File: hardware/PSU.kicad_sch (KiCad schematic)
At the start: 22 parts, among them J1 UJ20-C-H-G-SMT-2A-P16-TR, U2 REF35330QDBVR, U4 LM27762, U5 NCP1117-3.3_SOT223

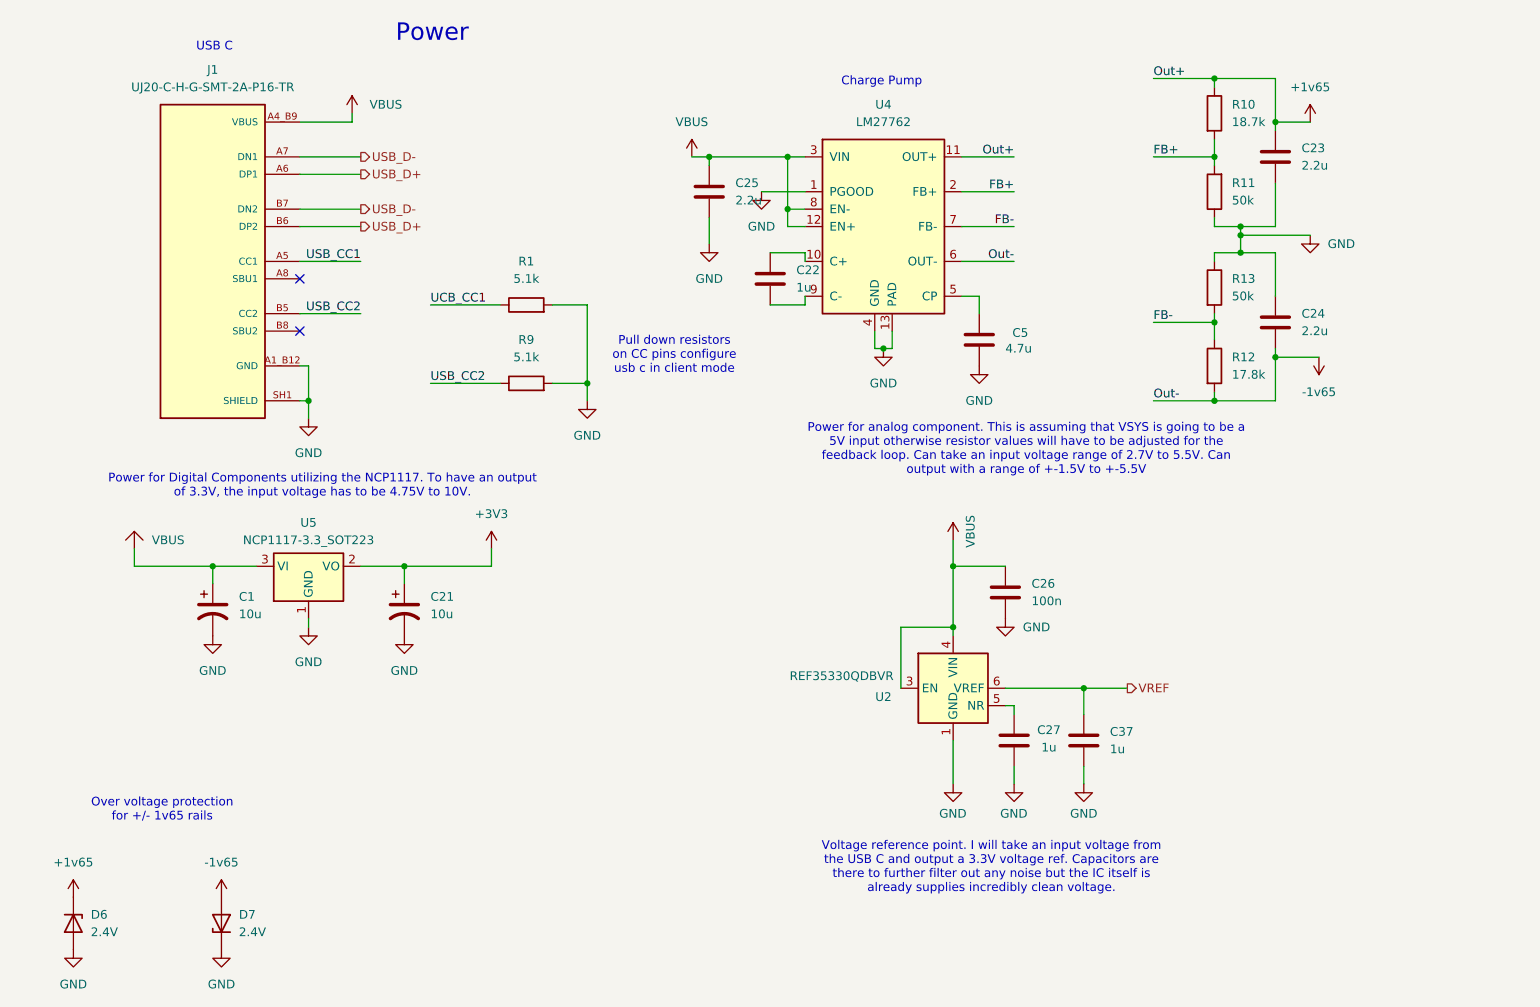
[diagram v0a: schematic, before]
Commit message: fix(hardware): Make power rail net naming consistent
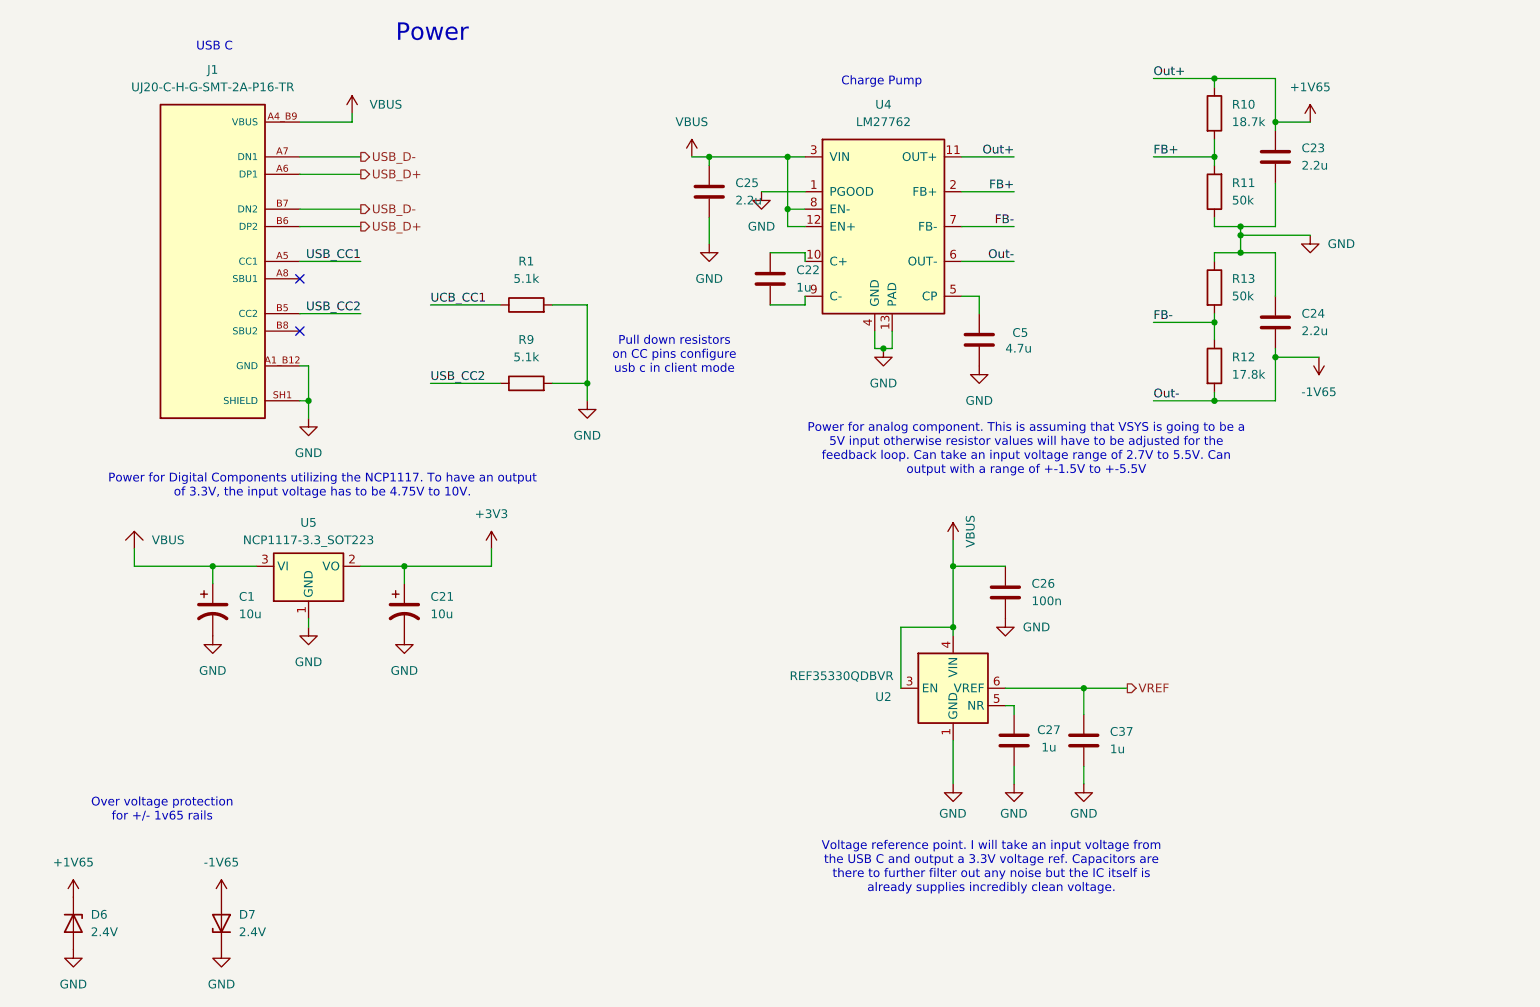
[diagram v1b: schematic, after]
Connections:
- net +1v65 renamed +1V65
- net -1v65 renamed -1V65
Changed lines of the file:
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@@
 			)
 		)
-		(property "Value" "+1v65"
+		(property "Value" "+1V65"
 			(at 231.14 43.18 0)
 			(effects
@@
 			)
 		)
-		(property "Value" "-1v65"
+		(property "Value" "-1V65"
 			(at 232.41 87.63 0)
 			(effects
@@
 			)
 		)
-		(property "Value" "+1v65"
+		(property "Value" "+1V65"
 			(at 50.8 156.21 0)
 			(effects
@@
 			)
 		)
-		(property "Value" "-1v65"
+		(property "Value" "-1V65"
 			(at 72.39 156.21 0)
 			(effects

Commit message: updated psu
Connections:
- net GND: no longer C23.2, C24.2, C25.2, C5.2, R11.1, R13.1, U4.13 (PAD), U4.4 (GND)
- new net GNDA: C23.2, C24.2, C25.2, C5.2, R11.1, R13.1, U4.13 (PAD), U4.4 (GND)
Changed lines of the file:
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@@
 			)
 		)
-		(property "Value" "GND"
+		(property "Value" "GNDA"
 			(at 233.68 66.0399 0)
 			(effects
@@
 			)
 		)
-		(property "Value" "GND"
-			(at 143.51 71.12 0)
-			(effects
-				(font
-					(size 1.27 1.27)
-				)
+		(property "Value" "GNDA"
+			(at 146.05 67.3099 0)
+			(effects
+				(font
+					(size 1.27 1.27)
+				)
+				(justify left)
 			)
 		)
@@
 			)
 		)
-		(property "Value" "GND"
-			(at 168.91 86.36 0)
-			(effects
-				(font
-					(size 1.27 1.27)
-				)
+		(property "Value" "GNDA"
+			(at 171.45 82.5499 0)
+			(effects
+				(font
+					(size 1.27 1.27)
+				)
+				(justify left)
 			)
 		)
@@
 			)
 		)
-		(property "Value" "GND"
-			(at 182.88 88.9 0)
-			(effects
-				(font
-					(size 1.27 1.27)
-				)
-			)
-		)
+		(property "Value" "GNDA"
+			(at 185.42 85.0899 0)
+			(effects
+				(font
+					(size 1.27 1.27)
+				)
+				(justify left)
+			)
+		)

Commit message: added footprints
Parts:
- C1, C21: footprint (none) -> Capacitor_SMD:C_1206_3216Metric
- C22, C23, C24, C25, C26, C27, C37, C5: footprint (none) -> Capacitor_SMD:C_0402_1005Metric
- D6, D7: footprint (none) -> Diode_SMD:D_SOD-123
- J1: footprint UJ20-C-H-G-SMT-1-P16-TR:SAMESKY_UJ20-C-H-G-SMT-1-P16-TR -> USBC_UJ20-C-H-G-SMT-1-P16-TR:SAMESKY_UJ20-C-H-G-SMT-1-P16-TR
- R1, R10, R11, R12, R13, R9: footprint (none) -> Resistor_SMD:R_0402_1005Metric
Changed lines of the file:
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@@
 			)
 		)
-		(property "Footprint" ""
+		(property "Footprint" "Diode_SMD:D_SOD-123"
 			(at 72.39 165.1 0)
 			(effects
@@
 			)
 		)
-		(property "Footprint" ""
+		(property "Footprint" "Capacitor_SMD:C_1206_3216Metric"
 			(at 71.12 119.38 0)
 			(effects
@@
 			)
 		)
-		(property "Footprint" ""
+		(property "Footprint" "Resistor_SMD:R_0402_1005Metric"
 			(at 116.84 76.708 90)
 			(effects
@@
 			)
 		)
-		(property "Footprint" ""
+		(property "Footprint" "Resistor_SMD:R_0402_1005Metric"
 			(at 215.392 72.39 90)
 			(effects
@@
 			)
 		)
-		(property "Footprint" ""
+		(property "Footprint" "Capacitor_SMD:C_0402_1005Metric"
 			(at 227.0252 57.15 0)
 			(effects
@@
 			)
 		)
-		(property "Footprint" ""
+		(property "Footprint" "Capacitor_SMD:C_0402_1005Metric"
 			(at 199.0852 142.24 0)
 			(effects
@@
 			)
 		)
-		(property "Footprint" ""
+		(property "Footprint" "Capacitor_SMD:C_0402_1005Metric"
 			(at 183.8452 83.82 0)
 			(effects
@@
 			)
 		)
-		(property "Footprint" ""
+		(property "Footprint" "Capacitor_SMD:C_0402_1005Metric"
 			(at 225.0948 73.66 0)
 			(effects
@@
 			)
 		)
-		(property "Footprint" "UJ20-C-H-G-SMT-1-P16-TR:SAMESKY_UJ20-C-H-G-SMT-1-P16-TR"
+		(property "Footprint" "USBC_UJ20-C-H-G-SMT-1-P16-TR:SAMESKY_UJ20-C-H-G-SMT-1-P16-TR"
 			(at 71.12 68.58 0)
 			(effects
@@
 			)
 		)
-		(property "Footprint" ""
+		(property "Footprint" "Capacitor_SMD:C_0402_1005Metric"
 			(at 186.9948 134.62 0)
 			(effects
@@
 			)
 		)
-		(property "Footprint" ""
+		(property "Footprint" "Resistor_SMD:R_0402_1005Metric"
 			(at 215.392 83.82 90)
 			(effects
@@
 			)
 		)
-		(property "Footprint" ""
+		(property "Footprint" "Capacitor_SMD:C_0402_1005Metric"
 			(at 144.4752 62.23 0)
 			(effects
@@
 			)
 		)
-		(property "Footprint" ""
+		(property "Footprint" "Resistor_SMD:R_0402_1005Metric"
 			(at 116.84 88.138 90)
 			(effects
@@
 			)
 		)
-		(property "Footprint" ""
+		(property "Footprint" "Capacitor_SMD:C_0402_1005Metric"
 			(at 187.6552 120.65 0)
 			(effects
@@
 			)
 		)
-		(property "Footprint" ""
+		(property "Footprint" "Capacitor_SMD:C_0402_1005Metric"
 			(at 153.3652 74.93 0)
 			(effects
@@
 			)
 		)
-		(property "Footprint" ""
+		(property "Footprint" "Resistor_SMD:R_0402_1005Metric"
 			(at 218.948 58.42 90)
 			(effects
@@
 			)
 		)
-		(property "Footprint" ""
+		(property "Footprint" "Resistor_SMD:R_0402_1005Metric"
 			(at 215.392 46.99 90)
 			(effects
@@
 			)
 		)
-		(property "Footprint" ""
+		(property "Footprint" "Capacitor_SMD:C_1206_3216Metric"
 			(at 99.06 119.38 0)
 			(effects
@@
 			)
 		)
-		(property "Footprint" ""
+		(property "Footprint" "Diode_SMD:D_SOD-123"
 			(at 50.8 165.1 0)
 			(effects

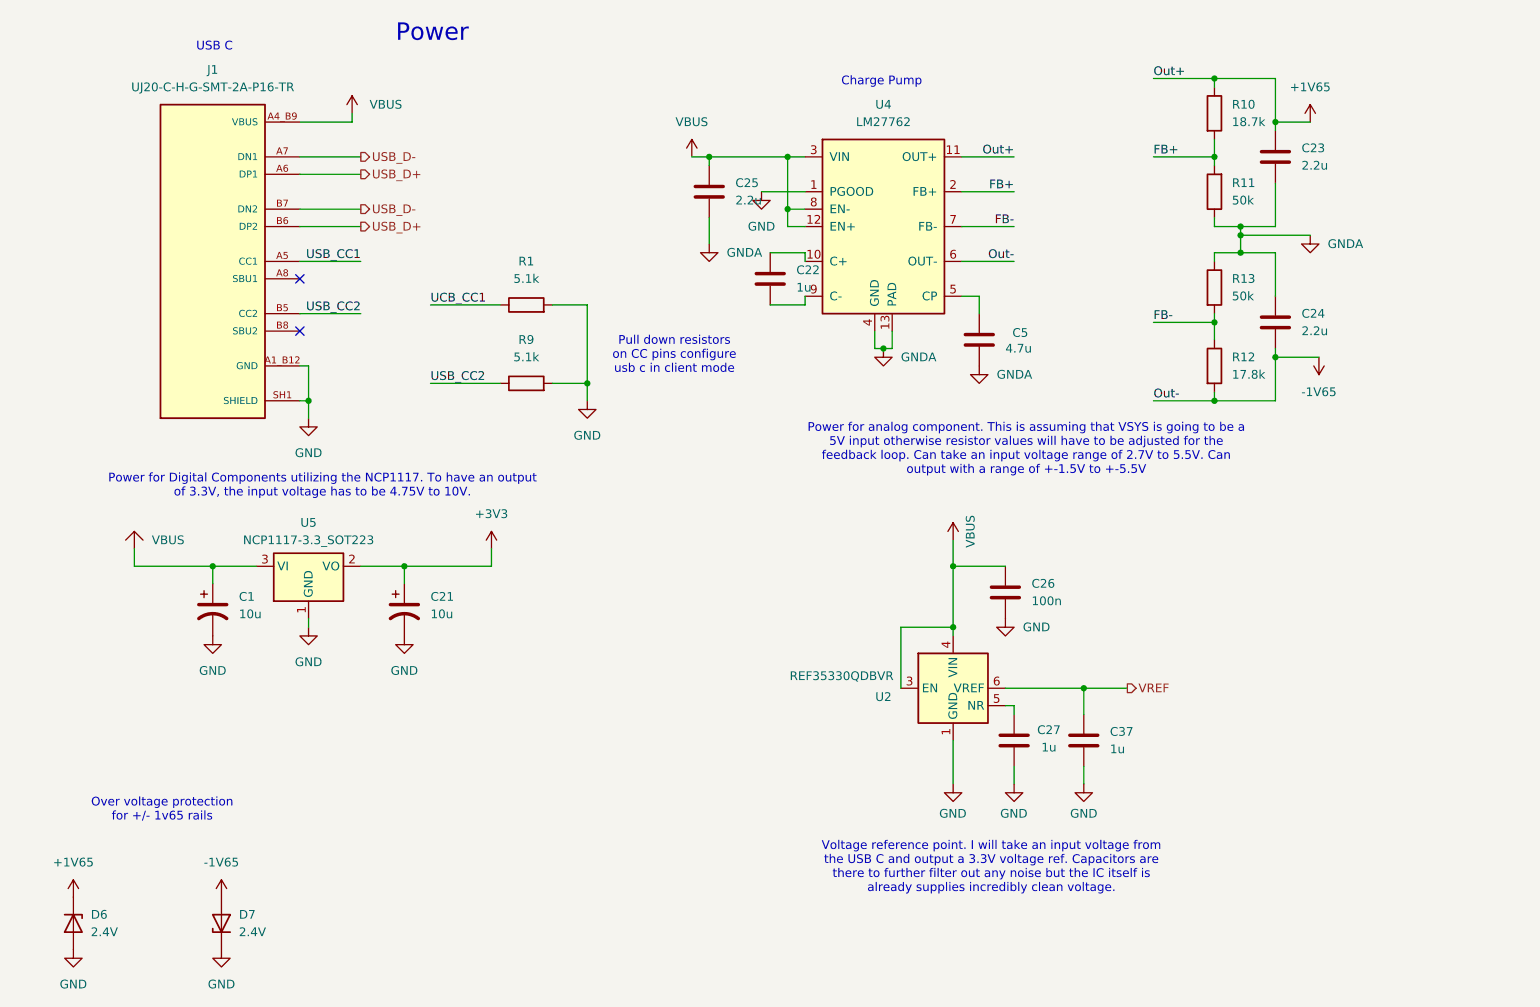
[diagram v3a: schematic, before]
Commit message: feat(hardware): Add test point connections + update PCB layout
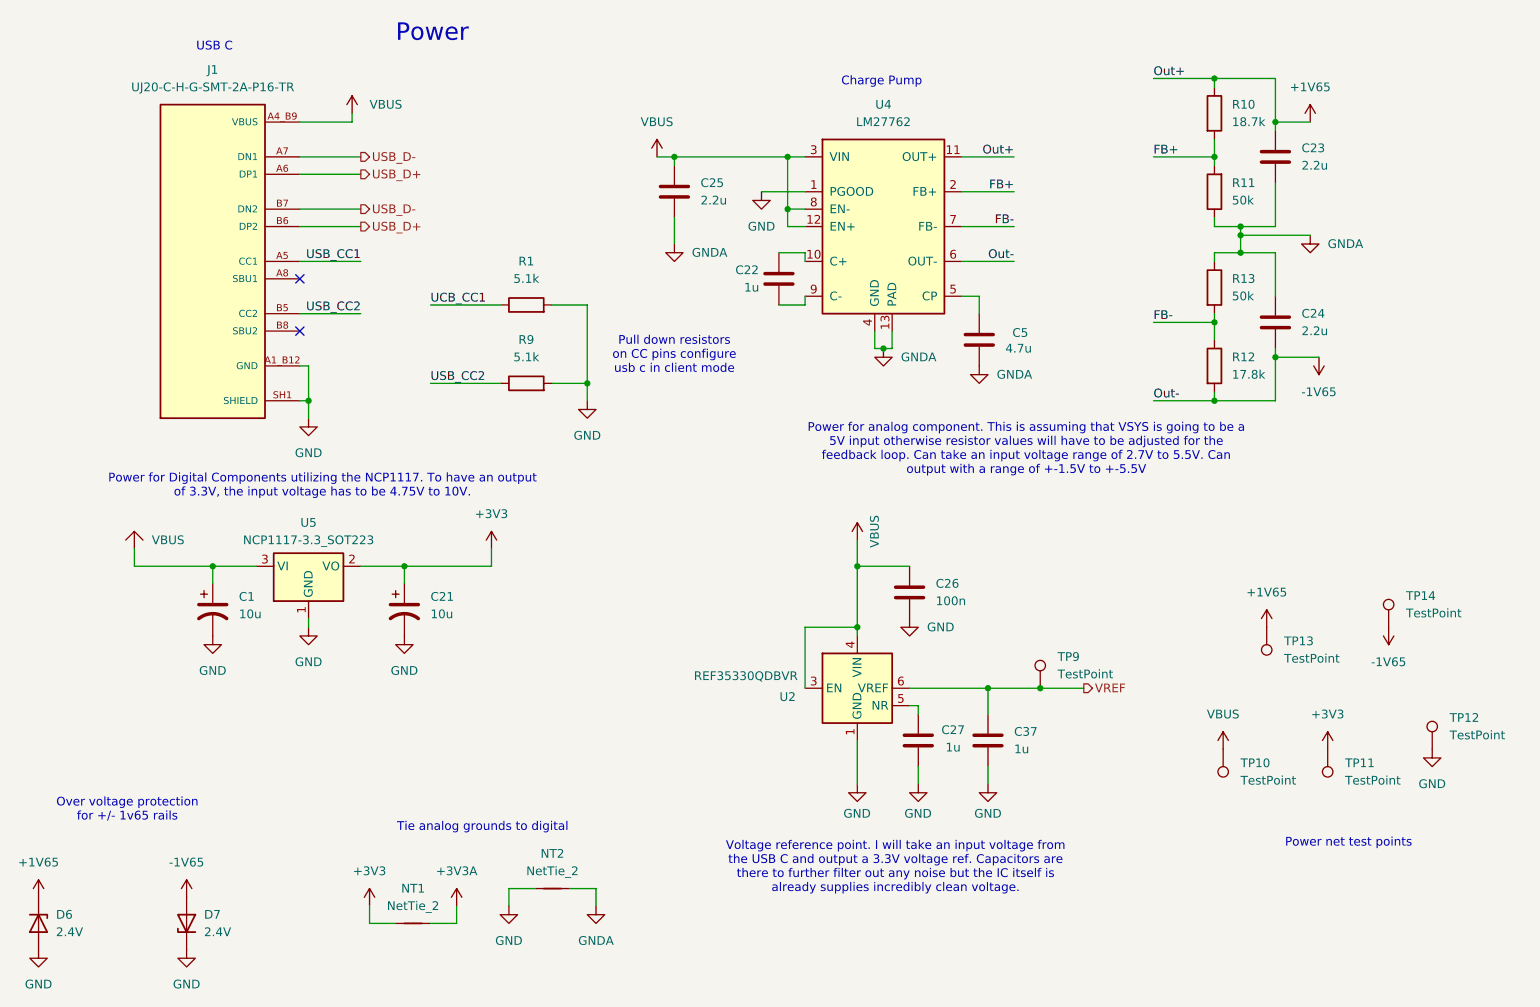
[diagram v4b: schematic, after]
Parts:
- added NT1, NT2: NetTie_2, NetTie:NetTie-2_SMD_Pad0.5mm, symbol Device:NetTie_2
- added TP10, TP11, TP12, TP13, TP14, TP9: TestPoint, CustomTestPoints:TestPoint_0603_1608Metric, symbol Connector:TestPoint
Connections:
- net +1V65: now also TP13.1
- net +3V3: now also NT1.1, TP11.1
- net -1V65: now also TP14.1
- net GND: now also NT2.1, TP12.1
- net GNDA: now also NT2.2
- net VBUS: now also TP10.1
- net VREF: now also TP9.1
- new net +3V3A: NT1.2
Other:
- note added: "Power net test points"
- note added: "Tie analog grounds to digital"
- moved on the sheet: C22, C25, C26, C27, C37, D6, D7, U2

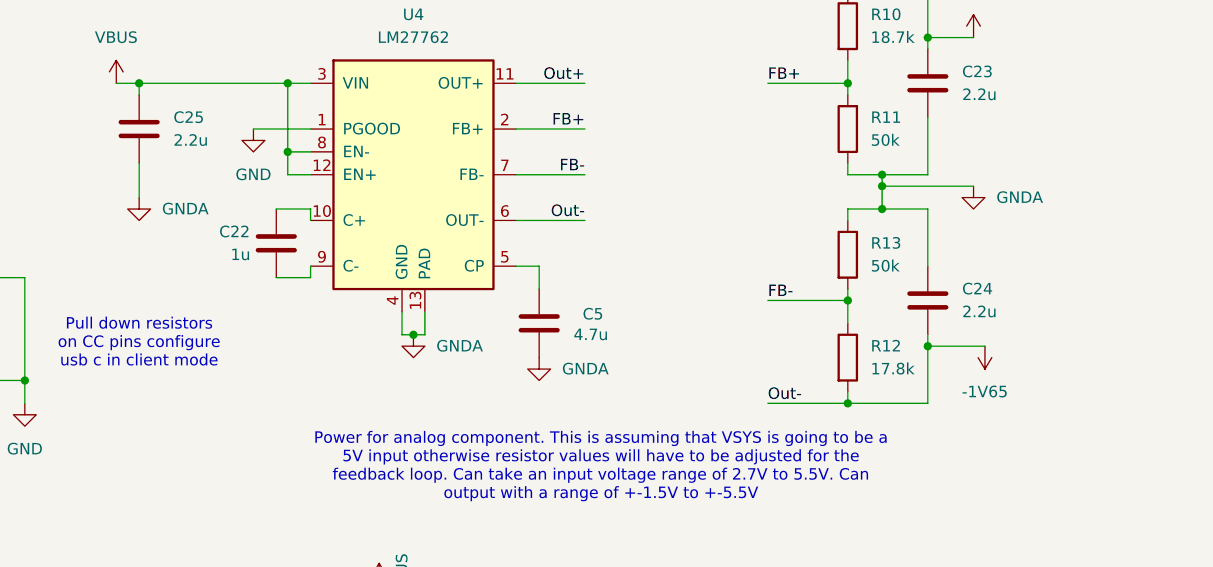
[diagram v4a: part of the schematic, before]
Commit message: feat(hardware): Update PCB layout for power and trigger blocks
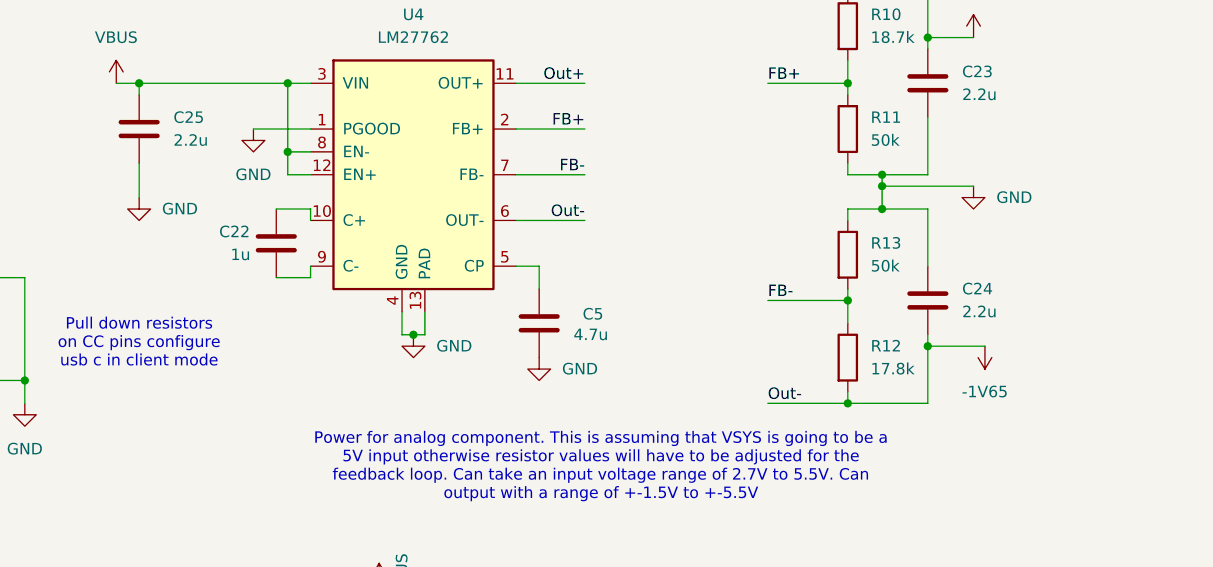
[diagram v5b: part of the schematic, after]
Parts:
- C1, C21: Price (none) -> $0.30; Purchase Link (none) -> https://www.digikey.com/en/products/detail/vishay-sprague/T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
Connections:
- net GND: now also C23.2, C24.2, C25.2, C5.2, R11.1, R13.1, U4.13 (PAD), U4.4 (GND)
- net GNDA: no longer C23.2, C24.2, C25.2, C5.2, R11.1, R13.1, U4.13 (PAD), U4.4 (GND)
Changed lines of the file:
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@@
 			)
 		)
+		(property "Price" "$0.30"
+			(at 71.12 119.38 0)
+			(effects
+				(font
+					(size 1.27 1.27)
+				)
+				(hide yes)
+			)
+		)
+		(property "Purchase Link" "https://www.digikey.com/en/products/detail/vishay-sprague/TMCHA1A106MTRF/10107267"
+			(at 71.12 119.38 0)
+			(effects
+				(font
+					(size 1.27 1.27)
+				)
+				(hide yes)
+			)
+		)
 		(pin "2"
 		)
@@
 			)
 		)
-		(property "Value" "GNDA"
+		(property "Value" "GND"
 			(at 233.68 66.0399 0)
 			(effects
@@
 			)
 		)
-		(property "Value" "GNDA"
+		(property "Value" "GND"
 			(at 140.97 67.3099 0)
 			(effects
@@
 			)
 		)
-		(property "Value" "GNDA"
+		(property "Value" "GND"
 			(at 171.45 82.5499 0)
 			(effects
@@
 			)
 		)
-		(property "Value" "GNDA"
+		(property "Value" "GND"
 			(at 185.42 85.0899 0)
 			(effects
@@
 			(at 99.06 119.38 0)
 			(effects
+				(font
+					(size 1.27 1.27)
+				)
+				(hide yes)
+			)
+		)
+		(property "Price" "$0.30"
+			(at 99.06 119.38 0)
+			(effects
+				(font
+					(size 1.27 1.27)
+				)
+				(hide yes)
+			)
+		)
+		(property "Purchase Link" "https://www.digikey.com/en/products/detail/vishay-sprague/TMCHA1A106MTRF/10107267"
+			(at 99.06 119.38 0)
+			(effects
